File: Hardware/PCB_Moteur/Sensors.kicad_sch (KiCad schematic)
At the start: 13 parts, among them J4 Conn_01x04_Socket, J5 Conn_01x04_Socket, U11 MAX6612MXK, U5 INA125UA/2K5, U6 INA125UA/2K5

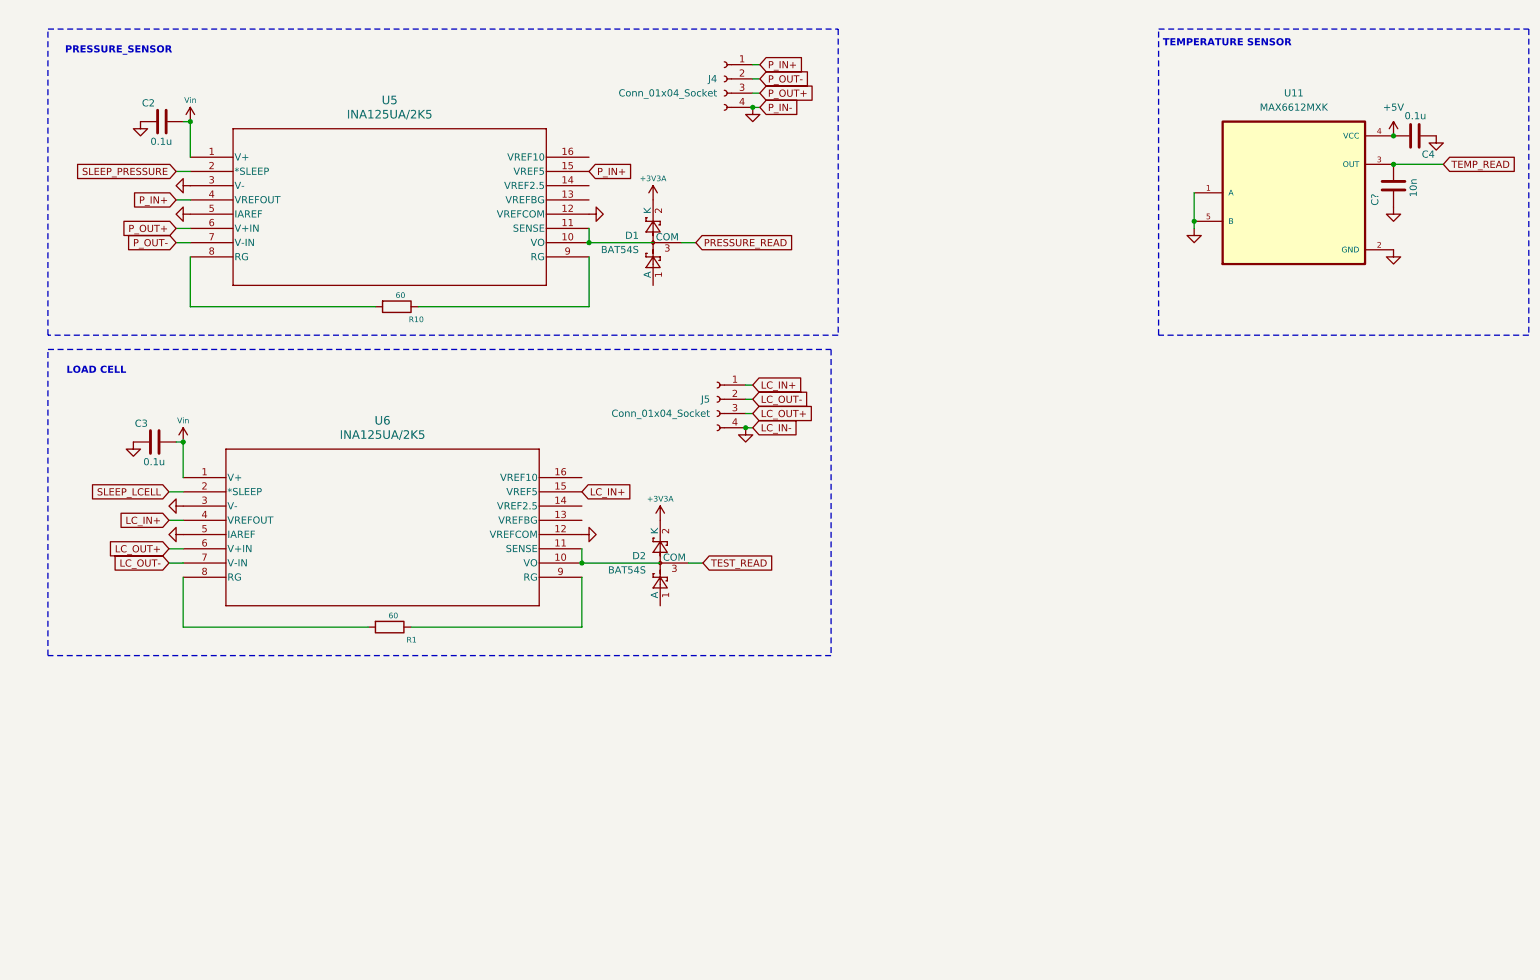
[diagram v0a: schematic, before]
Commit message: feat: setup stm32 project + mapping + add led LDO
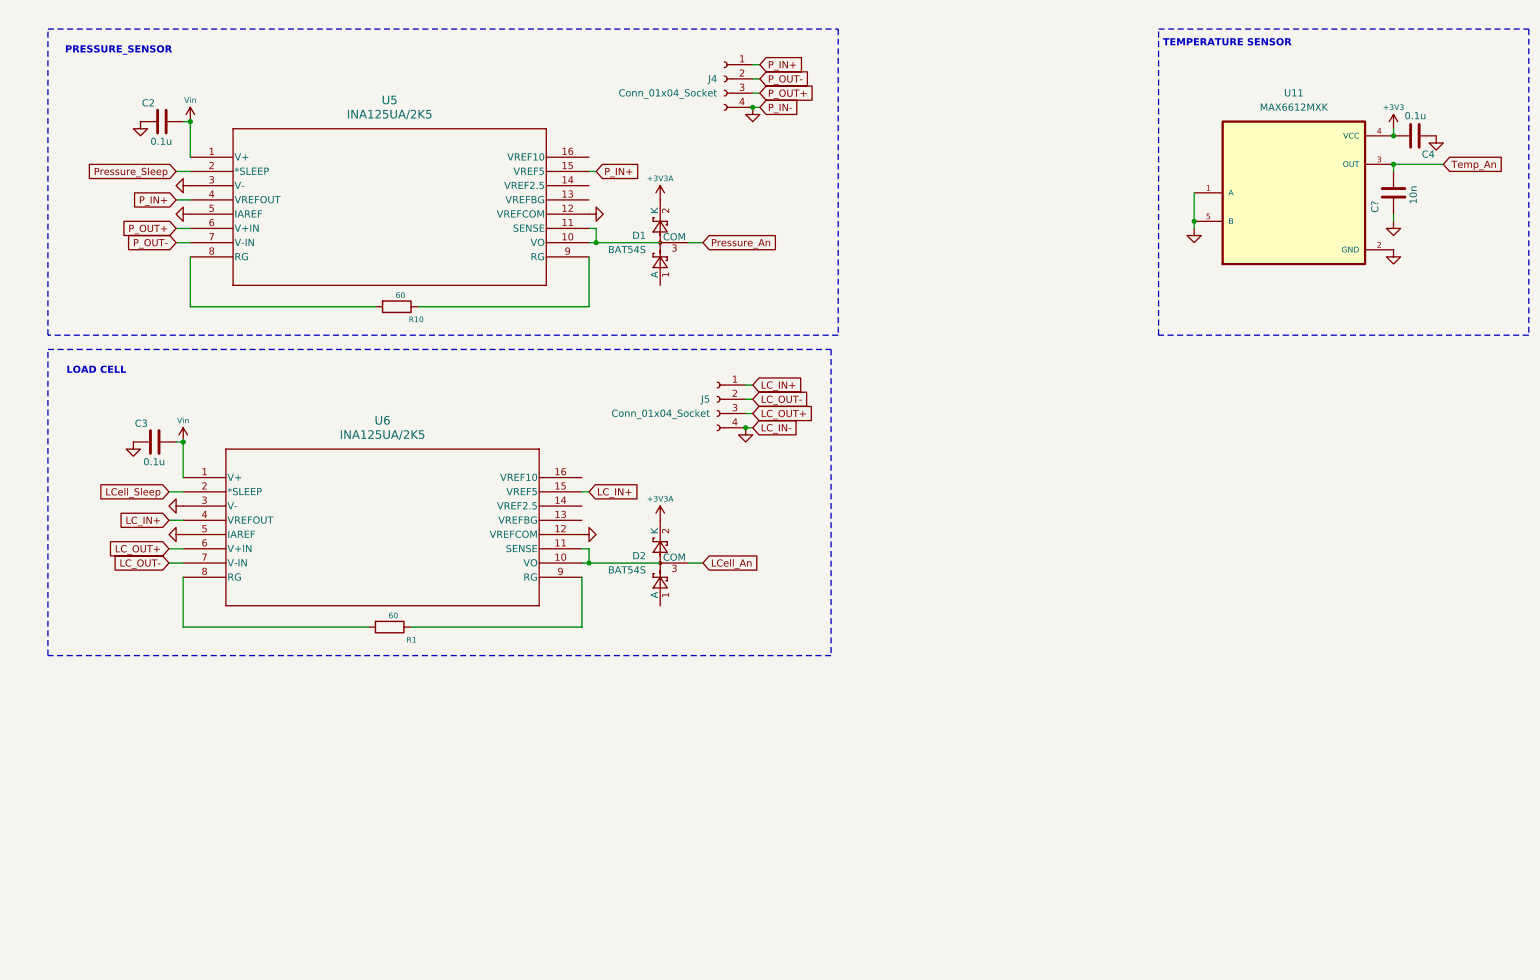
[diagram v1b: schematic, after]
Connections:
- net +5V renamed +3V3
- net PRESSURE_READ renamed Pressure_An
- net SLEEP_LCELL renamed LCell_Sleep
- net SLEEP_PRESSURE renamed Pressure_Sleep
- net TEMP_READ renamed Temp_An
- net TEST_READ renamed LCell_An
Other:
- moved on the sheet: C?, D1

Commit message: fix: LDO SHDN + complete stm32cubeide mapping (kicad missing) + add CAN in binary signal (connector missing)
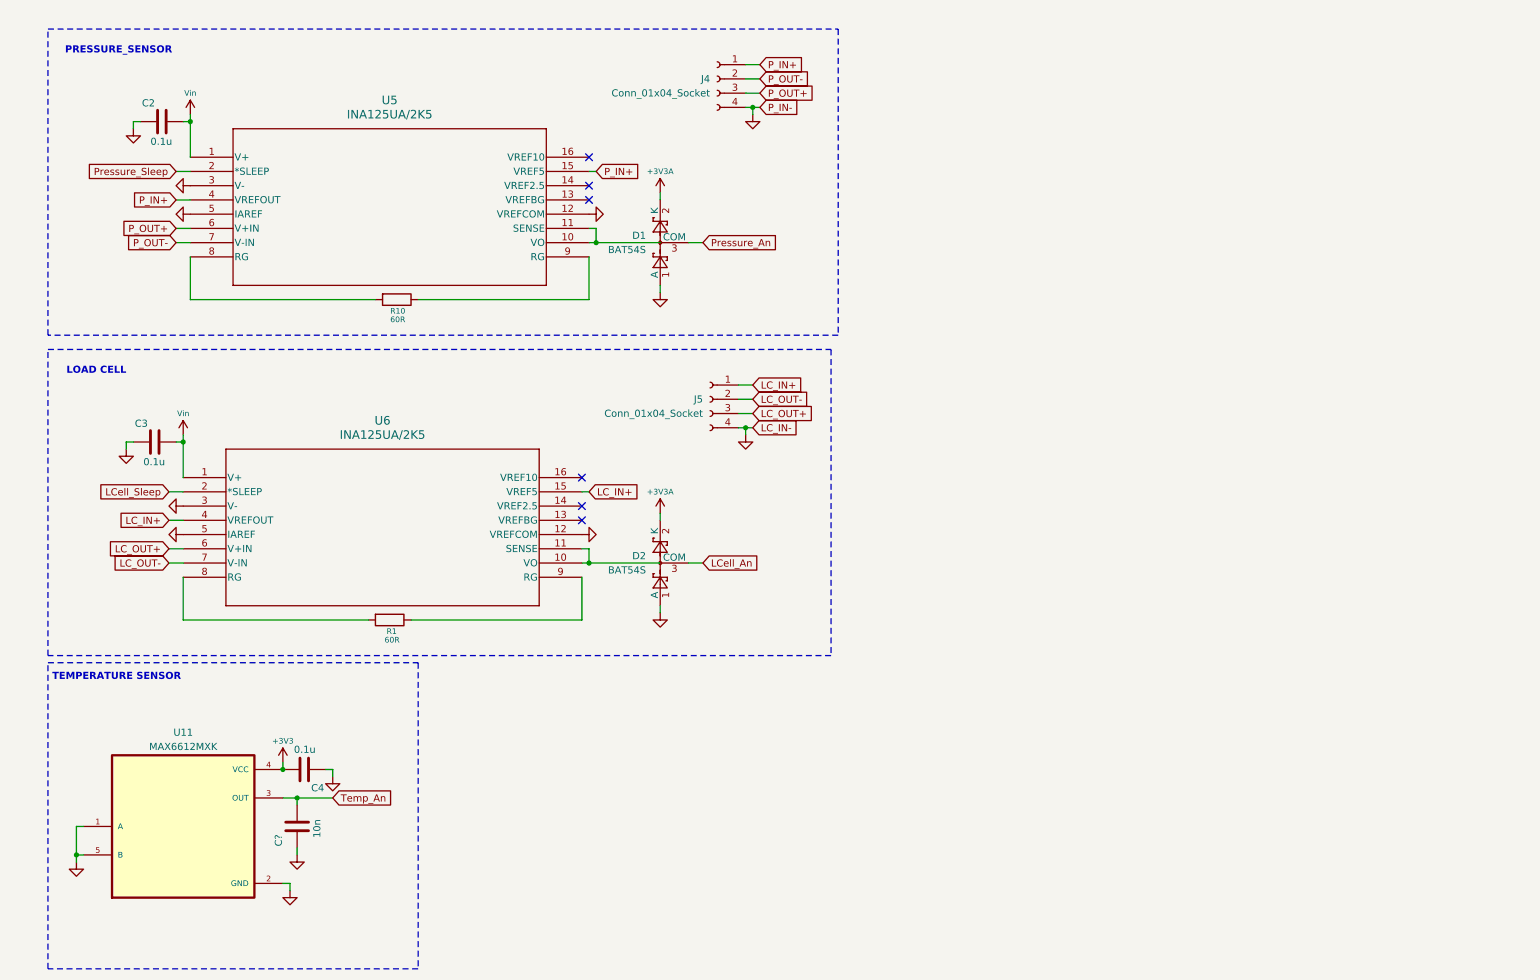
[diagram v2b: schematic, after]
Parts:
- R1, R10: value 60 -> 60R
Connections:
- net GND: now also D1.1 (A), D2.1 (A)
- no-connect marks 0 -> 6
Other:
- moved on the sheet: C4, C?, J4, J5, R1, R10, U11

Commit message: wip : pin mapping on STM32 and limit switch circuit
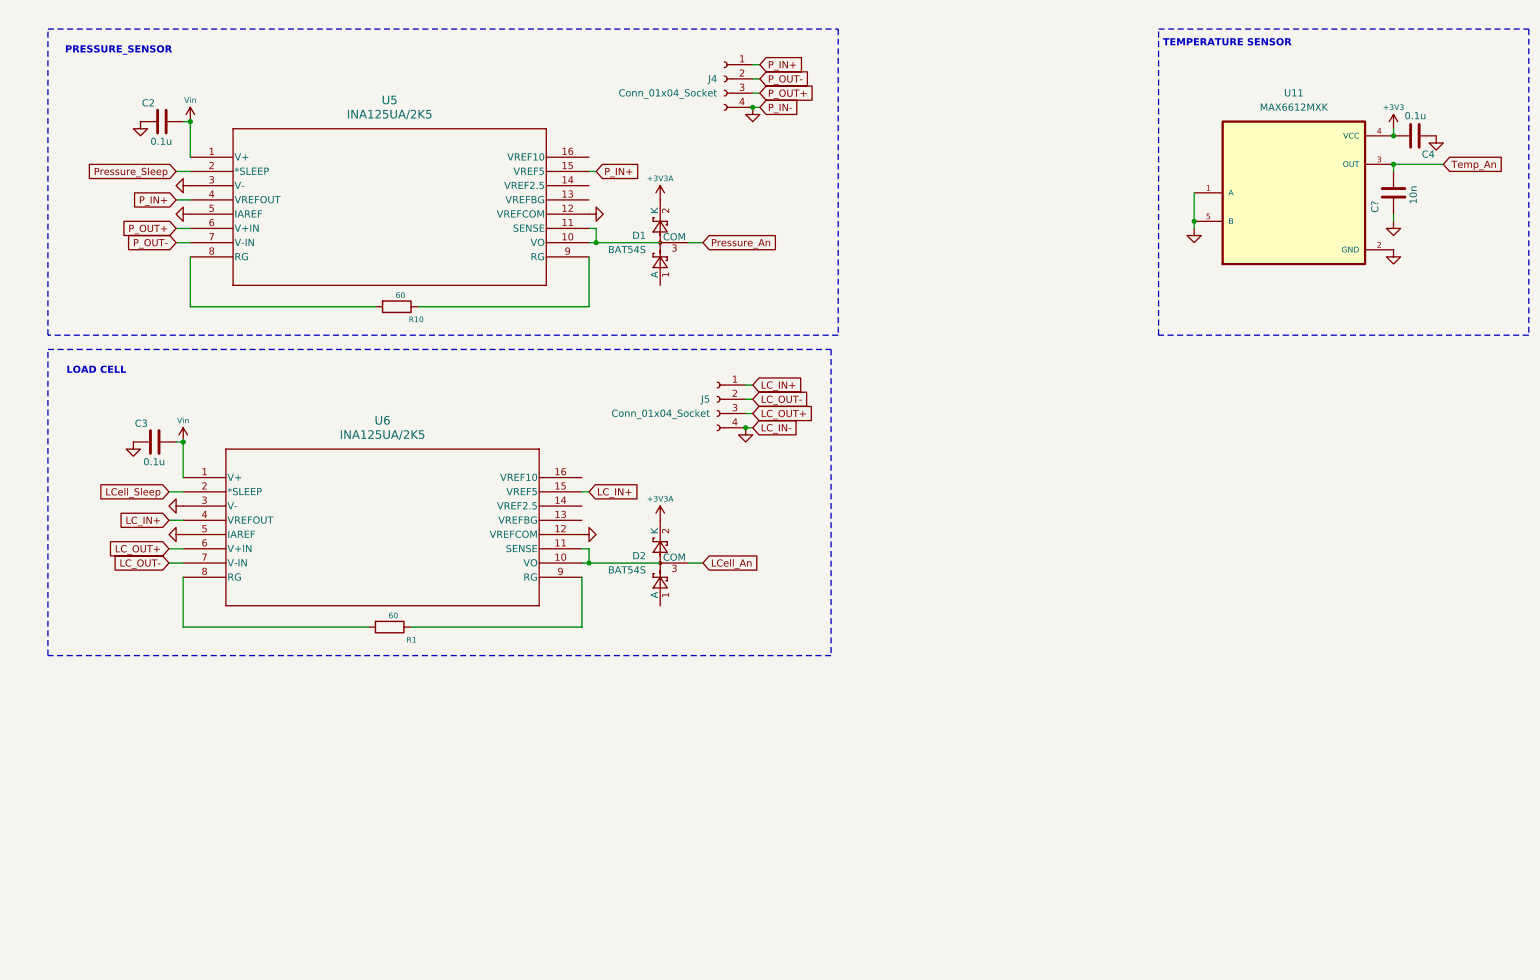
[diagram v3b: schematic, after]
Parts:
- R1, R10: value 60R -> 60
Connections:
- net GND: no longer D1.1 (A), D2.1 (A)
- no-connect marks 6 -> 0
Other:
- moved on the sheet: C4, C?, J4, J5, R1, R10, U11

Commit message: fix: LDO 5V SHDN + REFs (missing) + change EN valves controller connection + fix intrumental ampliop + add pull-down to sleep pins
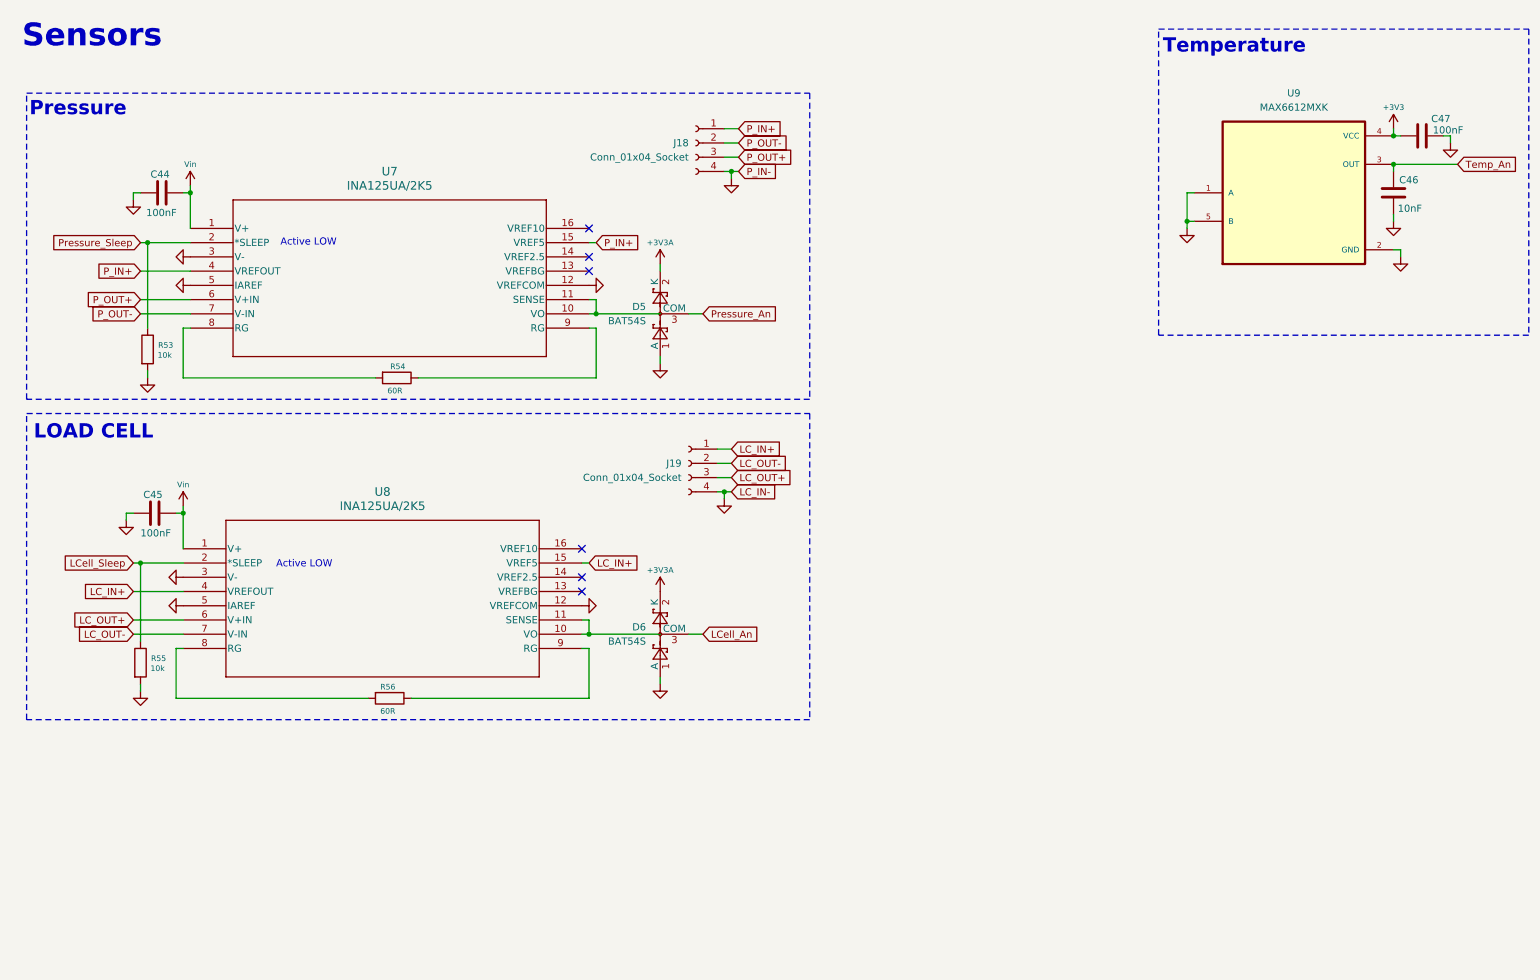
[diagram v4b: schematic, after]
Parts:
- added R53, R55: 10k, Resistor_SMD:R_0805_2012Metric, symbol Device:R
- C44: renamed from C2; value 0.1u -> 100nF
- C45: renamed from C3; value 0.1u -> 100nF
- C46: renamed from C?; value 10n -> 10nF
- C47: renamed from C4; value 0.1u -> 100nF
- R54: renamed from R10; value 60 -> 60R
- R56: renamed from R1; value 60 -> 60R
- renumbered D1 to D5, D2 to D6, J4 to J18, J5 to J19, U5 to U7, U6 to U8, U11 to U9
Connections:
- net GND: now also D5.1 (A), D6.1 (A), R53.2, R55.2
- net LCell_Sleep: now also R55.1
- net Pressure_Sleep: now also R53.1
- no-connect marks 0 -> 6
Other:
- note added: "Active LOW"
- note added: "Pressure"
- note added: "Sensors"
- note added: "Temperature"
- note removed: "PRESSURE_SENSOR"
- note removed: "TEMPERATURE SENSOR"
- moved on the sheet: C44, C45, C47, D5, D6, J18, J19, R54, R56, U7, U8

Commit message: Calculs gains, filtre rc
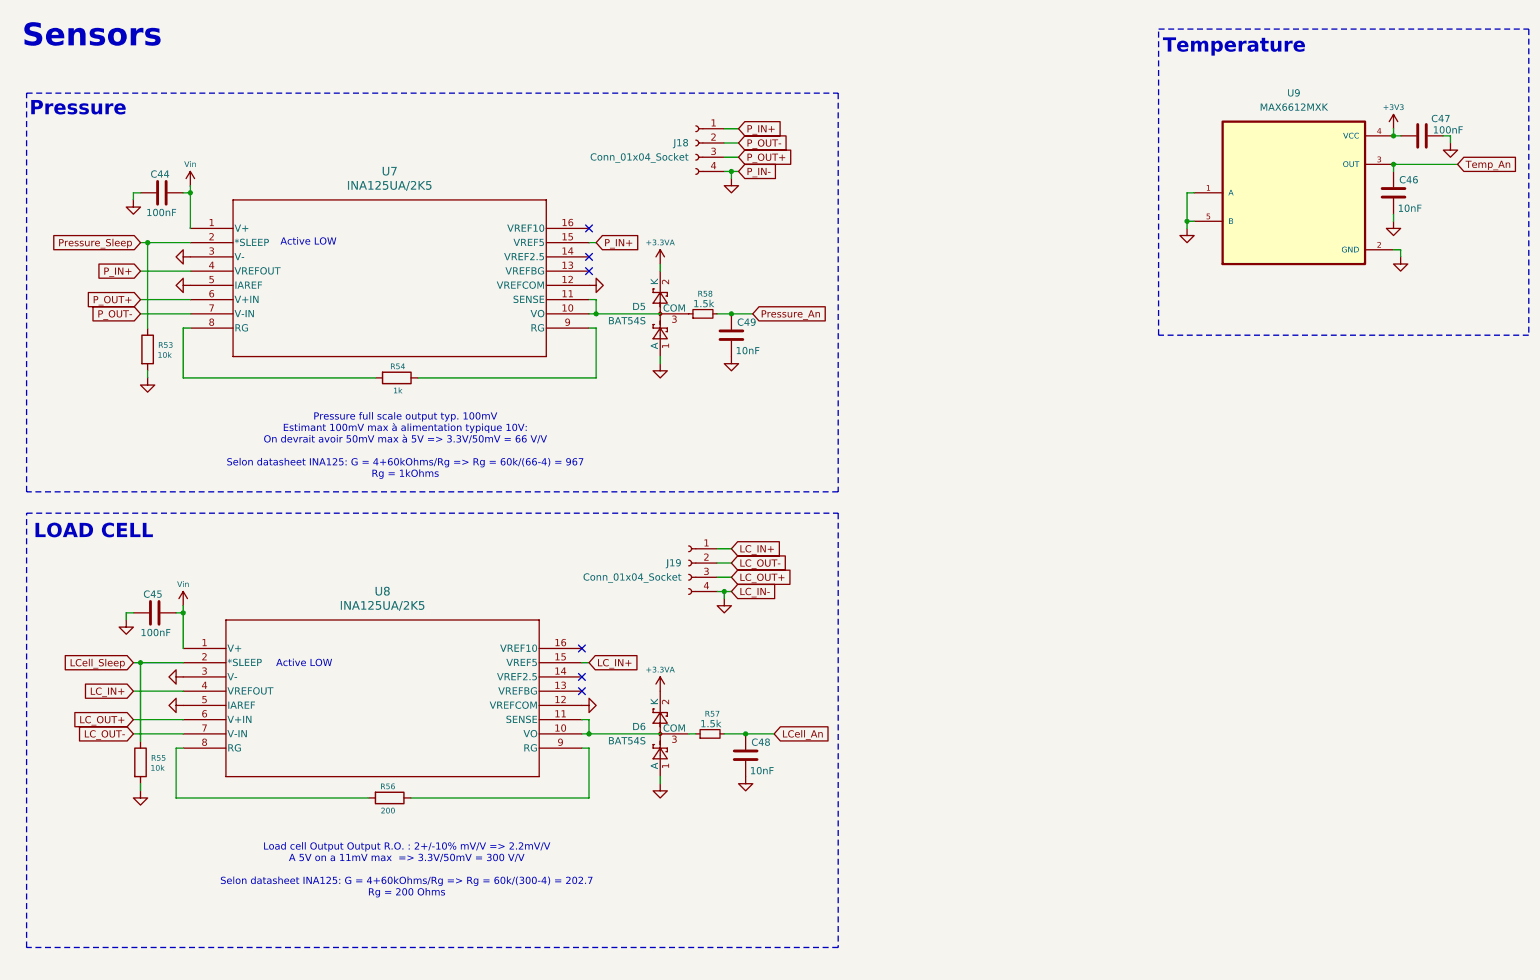
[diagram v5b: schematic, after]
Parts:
- added C48, C49: 10nF, symbol Device:C
- added R57, R58: 1.5k, Resistor_SMD:R_0603_1608Metric, symbol Device:R_Small
- R54: value 60R -> 1k
- R56: value 60R -> 200
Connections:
- net GND: now also C48.2, C49.2
- net LCell_An: now also C48.1, R57.2; no longer D6.3 (COM)
- net Pressure_An: now also C49.1, R58.2; no longer D5.3 (COM)
- net +3V3A renamed +3.3VA
- new net: D5.3 (COM), R58.1
- new net: D6.3 (COM), R57.1
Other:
- note added: "Load cell Output Output R.O. : 2+/-10% mV/V => 2.2mV/V A 5V on a 11mV max => 3.3V/50mV = 300 V/V Selon datasheet INA125: G = 4+60kOhms/Rg => Rg = 60k/(300-4) = 202.7 Rg = 200 Ohms"
- note added: "Pressure full scale output typ. 100mV Estimant 100mV max à alimentation typique 10V: On devrait avoir 50mV max à 5V => 3.3V/50mV = 66 V/V Selon datasheet INA125: G = 4+60kOhms/Rg => Rg = 60k/(66-4) = 967 Rg = 1kOhms"
- moved on the sheet: C45, D6, J19, R55, R56, U8
